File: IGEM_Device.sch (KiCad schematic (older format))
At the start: 17 parts, among them J1 67997-410HLF, U1 SaBLE-X-R2, U2 TC1014-2.85VCT713, U3 LMP91000SD_NOPB, U4 LM334MX_NOPB, U5 TPS79718QDCKRQ1

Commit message: s Please enter the commit message for your changes. Lines starting
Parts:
- added C6: 0.1u, symbol Device:C
- added J2: Conn_01x02, symbol Connector_Generic:Conn_01x02
- added J?: Conn_01x03, symbol Connector_Generic:Conn_01x03
- added U6: G-NIMO-003, SON50P250X250X75-9N, symbol IGEM_Device:G-NIMO-003
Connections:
- net +1V8: no longer U3.11 (VREF)
- net +2V85: now also C6.2, U6.1 (VDD)
- net COUN_ELECTRODE: now also J?.3 (Pin_3)
- net GND: now also C6.1, J2.1 (Pin_1), U6.4 (GND)
- net IP_CATHODE: now also J2.2 (Pin_2)
- net REF_ELECTRODE: now also J?.2 (Pin_2)
- net WORK_ELECTRODE: now also J?.1 (Pin_1)
- net POT_SCL renamed EXT_TEMP_SCL
- net EXT_TEMP_SCL: now also U6.2 (SCL)
- net POT_SDA renamed EXT_TEMP_SDA
- net EXT_TEMP_SDA: now also U6.3 (SDA)
- no-connect marks 17 -> 18
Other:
- moved on the sheet: C1, C2, C3, D1, R3, R5, U2, U3, U4

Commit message: schem v2.2
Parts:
- removed J2: Conn_01x02, symbol Connector_Generic:Conn_01x02
- removed J?: Conn_01x03, symbol Connector_Generic:Conn_01x03
- added C10, C11: 1u, symbol Device:C
- added C7, C8, C9: 0.1u, symbol Device:C
- added J2: Conn_01x05, symbol Connector_Generic:Conn_01x05
- added J3: Batt_Conn, symbol Connector_Generic:Conn_01x02
- added SW1: Power_Switch, symbol Switch:SW_DIP_x01
- R1, R2: value 100k -> 10k
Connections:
- net +1V8: now also U3.11 (VREF), C9.1
- net +2V85: now also C10.1, C7.1, C8.1
- net +BATT: now also C11.1, J3.1 (Pin_1), SW1.1; no longer C3.1, U2.1 (VIN), U2.3 (~SHDN)
- net COUN_ELECTRODE: now also J2.4 (Pin_4)
- net GND: now also C10.2, C11.2, C7.2, C8.2, C9.2, J2.5 (Pin_5)
- net IP_CATHODE: now also J2.1 (Pin_1)
- net REF_ELECTRODE: now also J2.3 (Pin_3)
- net WORK_ELECTRODE: now also J2.2 (Pin_2)
- new net: C3.1, SW1.2, U2.1 (VIN), U2.3 (~SHDN)
- new net -BATT: J3.2 (Pin_2)
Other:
- moved on the sheet: C1, C2, C3, C4, C5, C6, D1, J1, R1, R2, R3, R4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

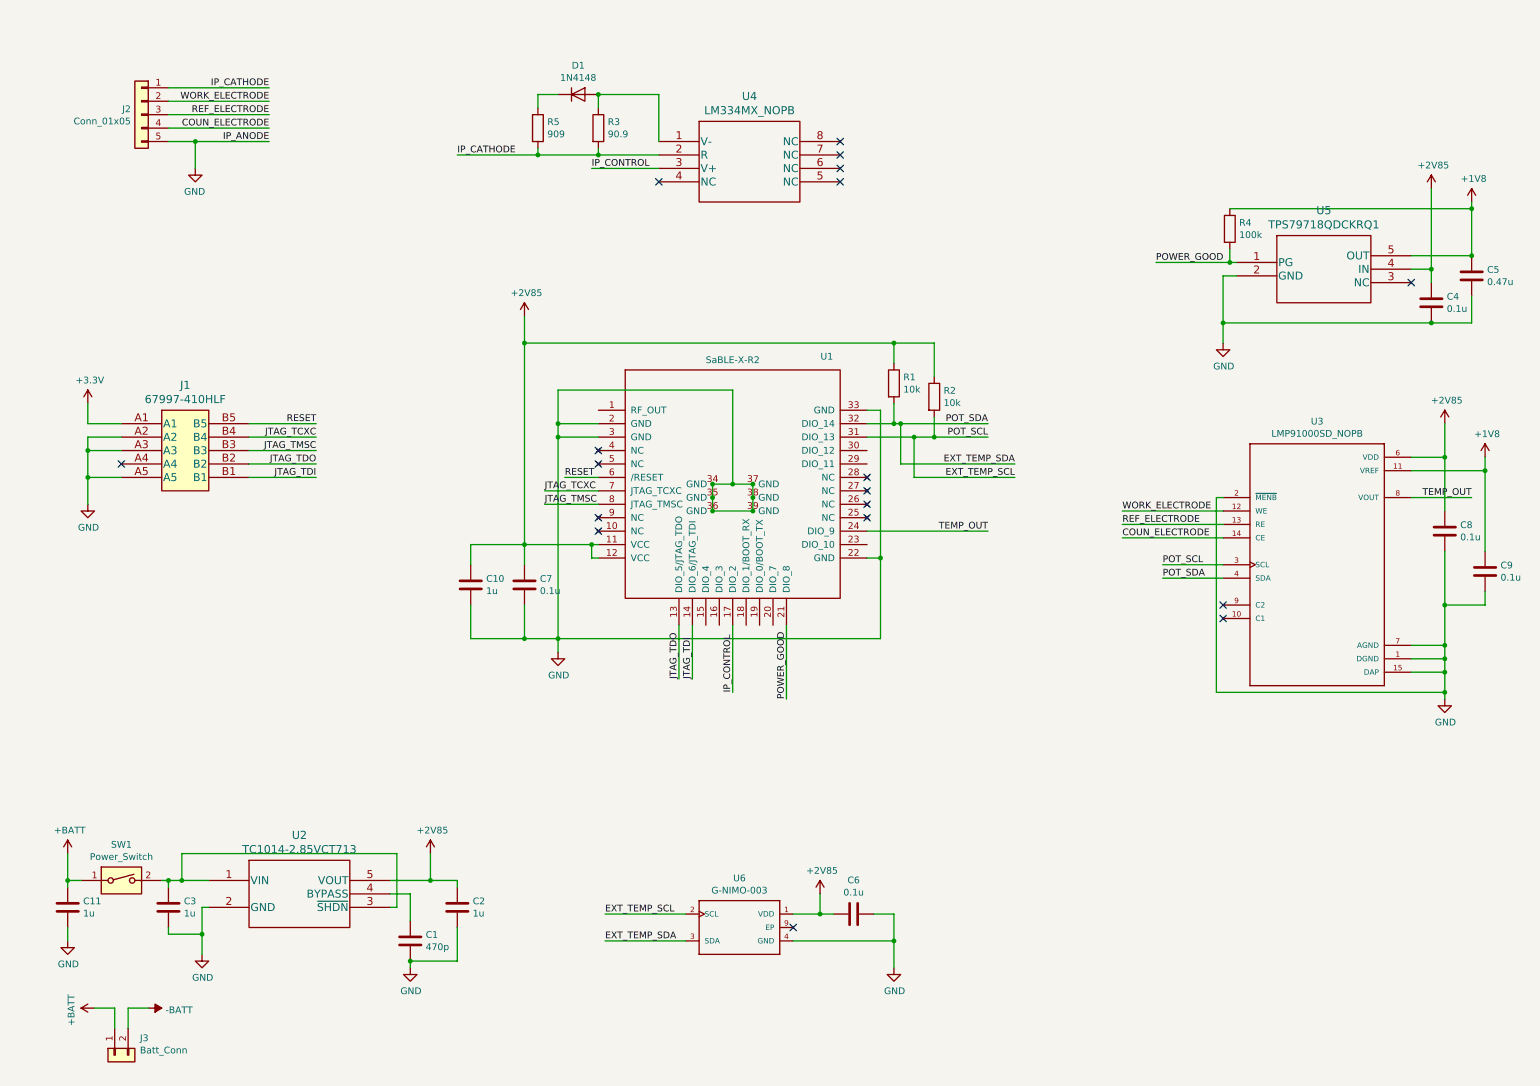
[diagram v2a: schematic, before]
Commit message: Associated most footprints to their symbols
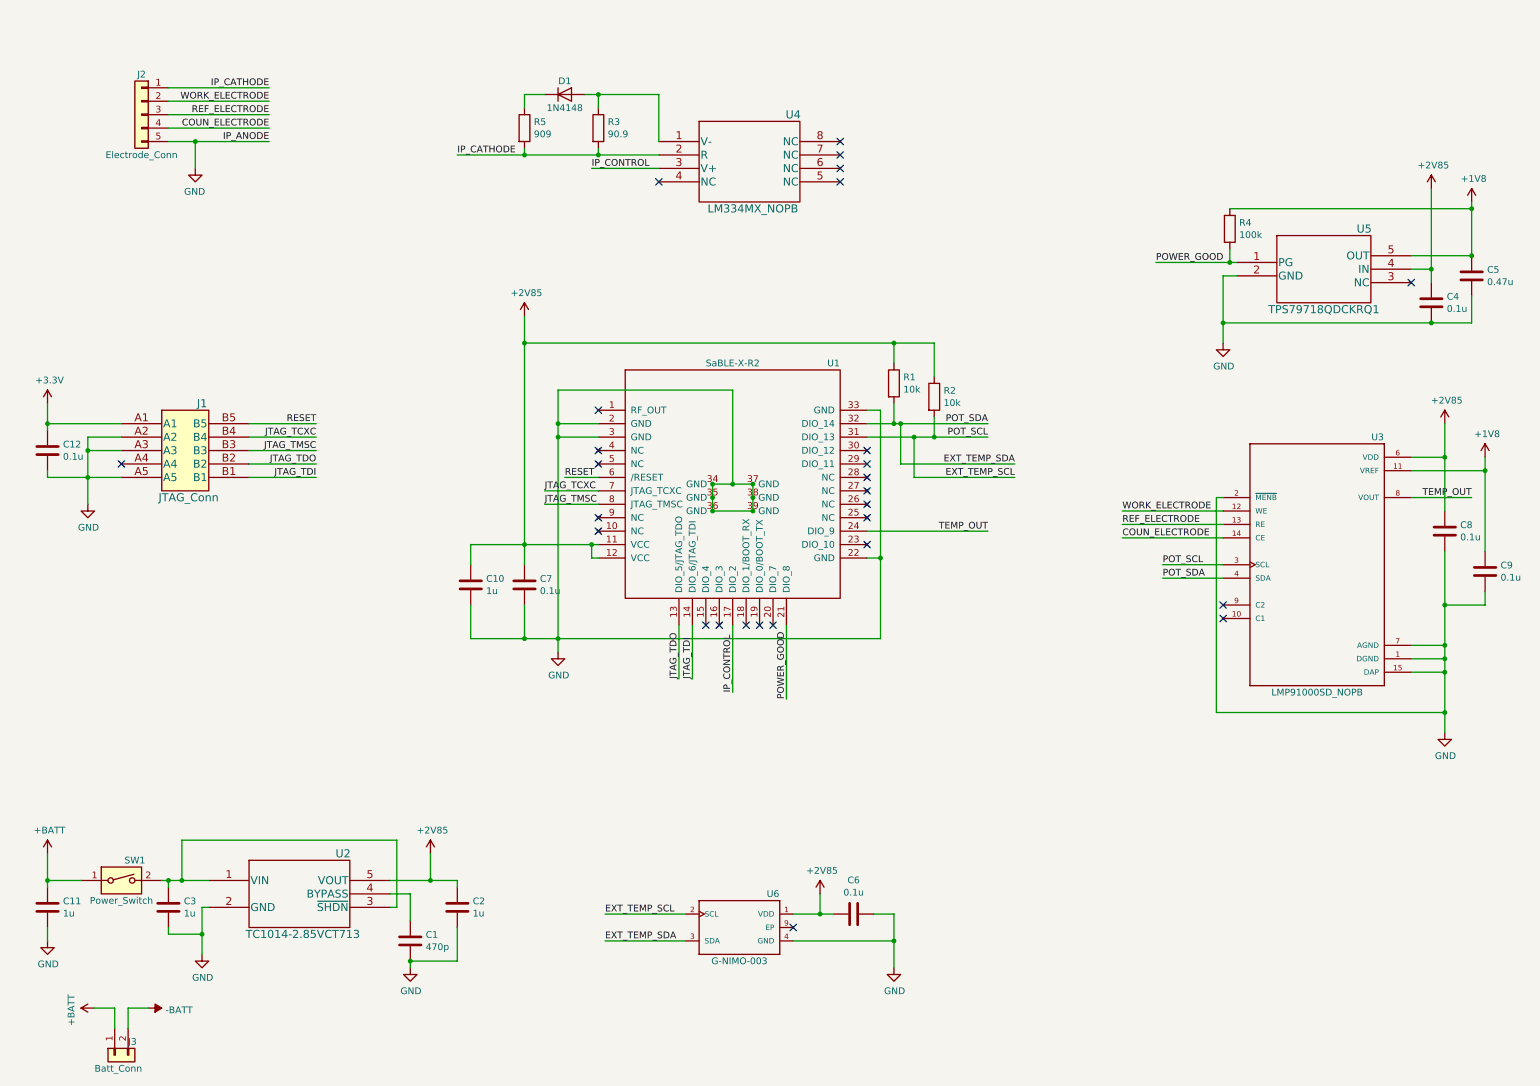
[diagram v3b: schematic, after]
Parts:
- added C12: 0.1u, Capacitors_SMD:C_0805, symbol Device:C
- C1, C10, C11, C2, C3, C4, C5, C6, C7, C8, C9: footprint (none) -> Capacitors_SMD:C_0805
- D1: footprint Diode_THT:D_DO-35_SOD27_P7.62mm_Horizontal -> (none)
- J1: value 67997-410HLF -> JTAG_Conn; footprint 10 Pins -> (none)
- J2: value Conn_01x05 -> Electrode_Conn
- R1, R2, R3, R4, R5: footprint (none) -> Resistors_SMD:R_0805
- U2: footprint SOT-23-5_MC -> (none)
- U3: footprint SON50P400X400X80-15N -> (none)
- U4: footprint M08A -> (none)
- U5: footprint DCK5 -> (none)
- U6: footprint SON50P250X250X75-9N -> (none)
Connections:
- net +3V3: now also C12.1
- net GND: now also C12.2
- no-connect marks 18 -> 27
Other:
- moved on the sheet: C11, D1, R5
